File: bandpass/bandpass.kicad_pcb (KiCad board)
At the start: 2 copper layers, 100 x 100 mm, 24 parts, among them J1 RX, J3 Conn_Coaxial, K2 G6K-2, K3 G6K-2, K4 G6K-2, K5 G6K-2, K6 G6K-2, K7 G6K-2, K8 G6K-2, P1 PMOD-Device-x2-Type-Generic-A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

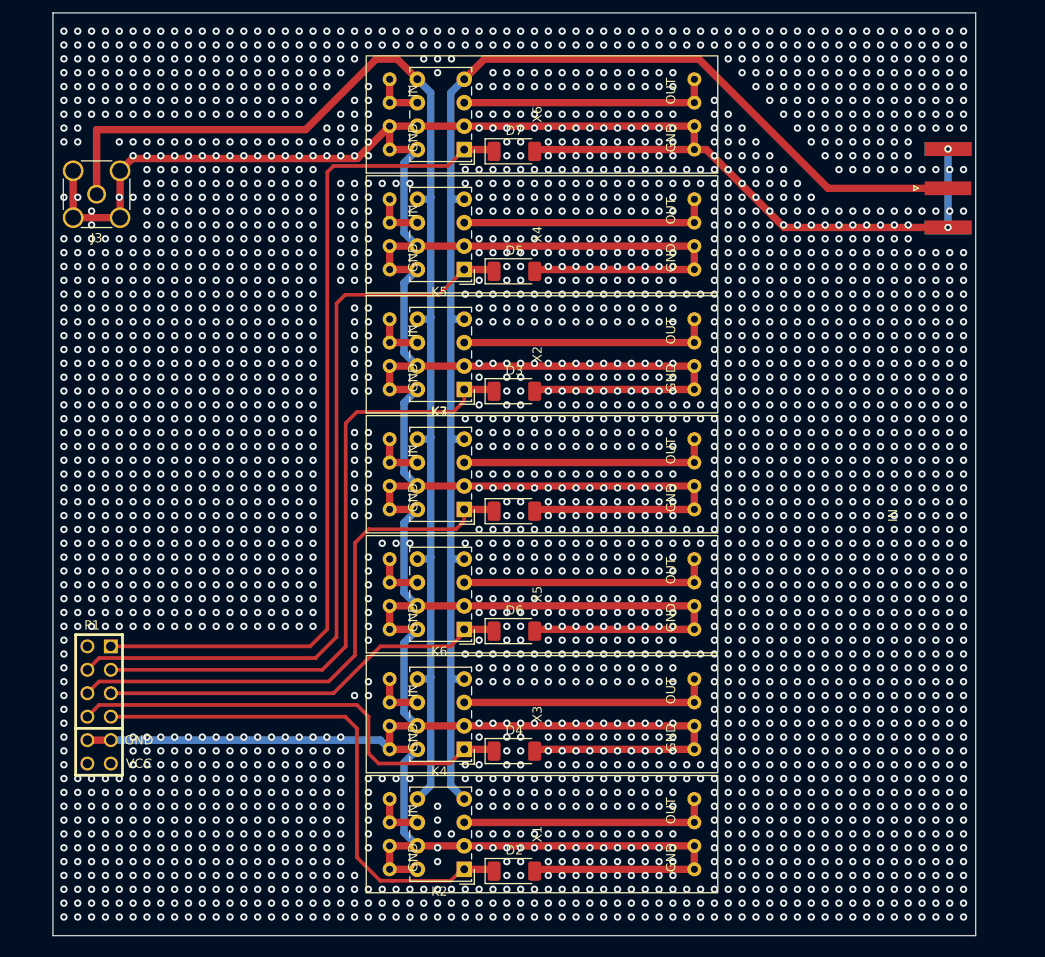
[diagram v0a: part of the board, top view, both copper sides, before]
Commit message: replace RF connectors, add missing silkscreen text
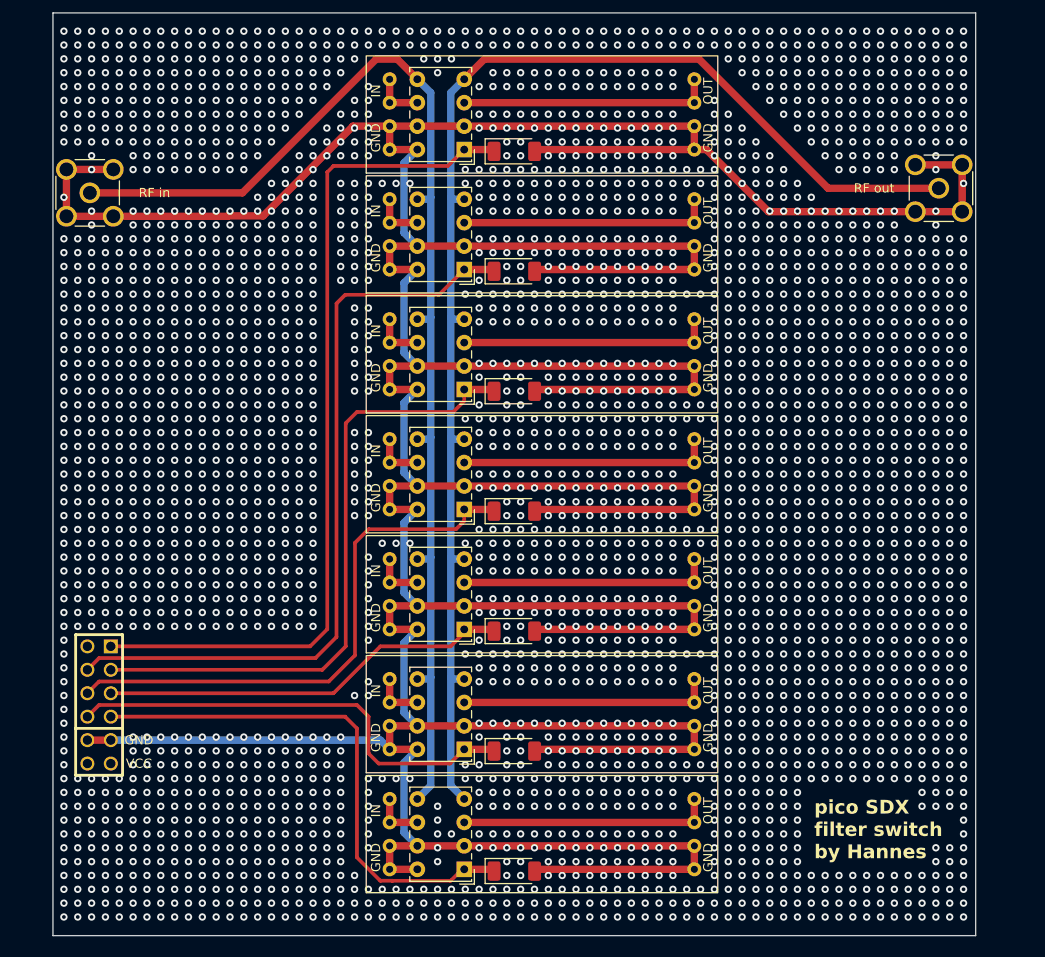
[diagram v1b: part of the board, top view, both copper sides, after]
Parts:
- J1: footprint Connector_Coaxial:SMA_Amphenol_132289_EdgeMount -> Connector_Coaxial:SMA_Molex_73251-2200_Horizontal
- J3: footprint Connector_Coaxial:SMA_Amphenol_132291_Vertical -> Connector_Coaxial:SMA_Molex_73251-2200_Horizontal
- moved J1 1.00 mm to (111.7, 36.2), turned to -90 degrees
- moved J3 0.75 mm to (19.7, 36.7), turned to 90 degrees
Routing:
- net GND: track 598.5 -> 603.8 mm, vias 3231 -> 3170
- net /Bandpass Filter/RF out: track 132.7 -> 129.2 mm
- net /Bandpass Filter/RF in: track 146.0 -> 145.0 mm
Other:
- board text added: "RF in"
- board text added: "RF out"
- board text added: "pico SDX filter switch by Hannes"

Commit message: drc clean
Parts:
- moved J1 1.00 mm to (110.7, 36.2)
- moved J3 0.92 mm to (20.7, 36.7)
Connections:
- D2 pad 1: 40 m -> +12V
- D2 pad 2: GND -> 40 m
- D3 pad 1: 15 m -> +12V
- D3 pad 2: GND -> 15 m
- D4 pad 1: 30 m -> +12V
- D4 pad 2: GND -> 30 m
- D5 pad 1: 12 m -> +12V
- D5 pad 2: GND -> 12 m
- D6 pad 1: 20 m -> +12V
- D6 pad 2: GND -> 20 m
- D7 pad 1: 10 m -> +12V
- D7 pad 2: GND -> 10 m
- D8 pad 1: 17 m -> +12V
- D8 pad 2: GND -> 17 m
- K2 pad 1: 40 m -> +12V
- K2 pad 8: GND -> 40 m
- K3 pad 1: 15 m -> +12V
- K3 pad 8: GND -> 15 m
- K4 pad 1: 30 m -> +12V
- K4 pad 8: GND -> 30 m
- K5 pad 1: 12 m -> +12V
- K5 pad 8: GND -> 12 m
- K6 pad 1: 20 m -> +12V
- K6 pad 8: GND -> 20 m
- K7 pad 1: 10 m -> +12V
- K7 pad 8: GND -> 10 m
- K8 pad 1: 17 m -> +12V
- K8 pad 8: GND -> 17 m
- P1 pad 12: unconnected-(P1-P12-Pad12) -> +12V
- P1 pad 6: unconnected-(P1-P6-Pad6) -> +12V
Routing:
- net +12V: track 0.00 -> 155.8 mm
- net GND: track 603.8 -> 473.8 mm, vias 3170 -> 6833
- net 12 m: track 83.3 -> 89.2 mm
- net 10 m: track 92.9 -> 98.8 mm
- net 30 m: track 50.3 -> 56.2 mm
- net 40 m: track 57.7 -> 63.5 mm
- net 20 m: track 44.7 -> 50.3 mm
- net 17 m: track 60.3 -> 65.4 mm
- net 15 m: track 69.1 -> 74.2 mm
- net /Bandpass Filter/RF in: track 145.0 -> 144.0 mm
- net /Bandpass Filter/RF out: track 129.2 -> 128.3 mm
